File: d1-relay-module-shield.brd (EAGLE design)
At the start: 26.6 x 28.9 mm, 5 parts

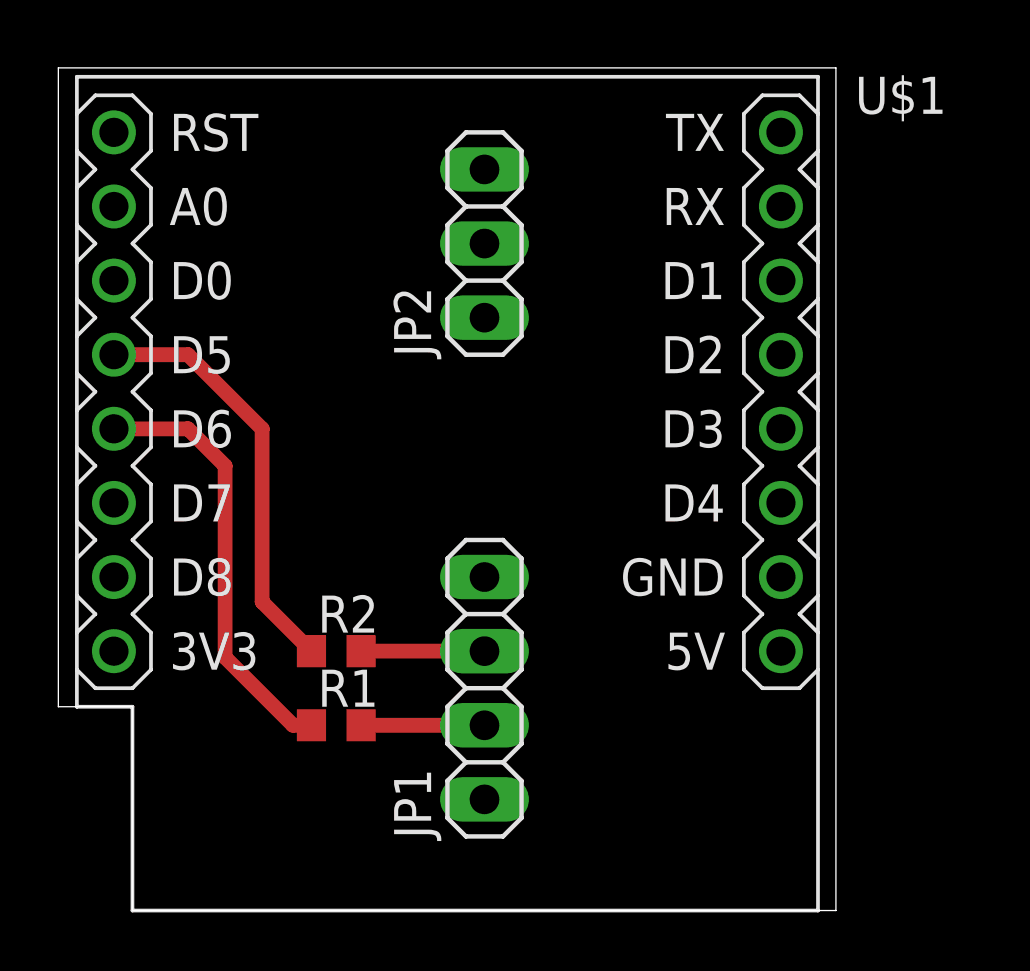
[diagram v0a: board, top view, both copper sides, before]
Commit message: align d1 with edge of relay board and add cutout for jumper
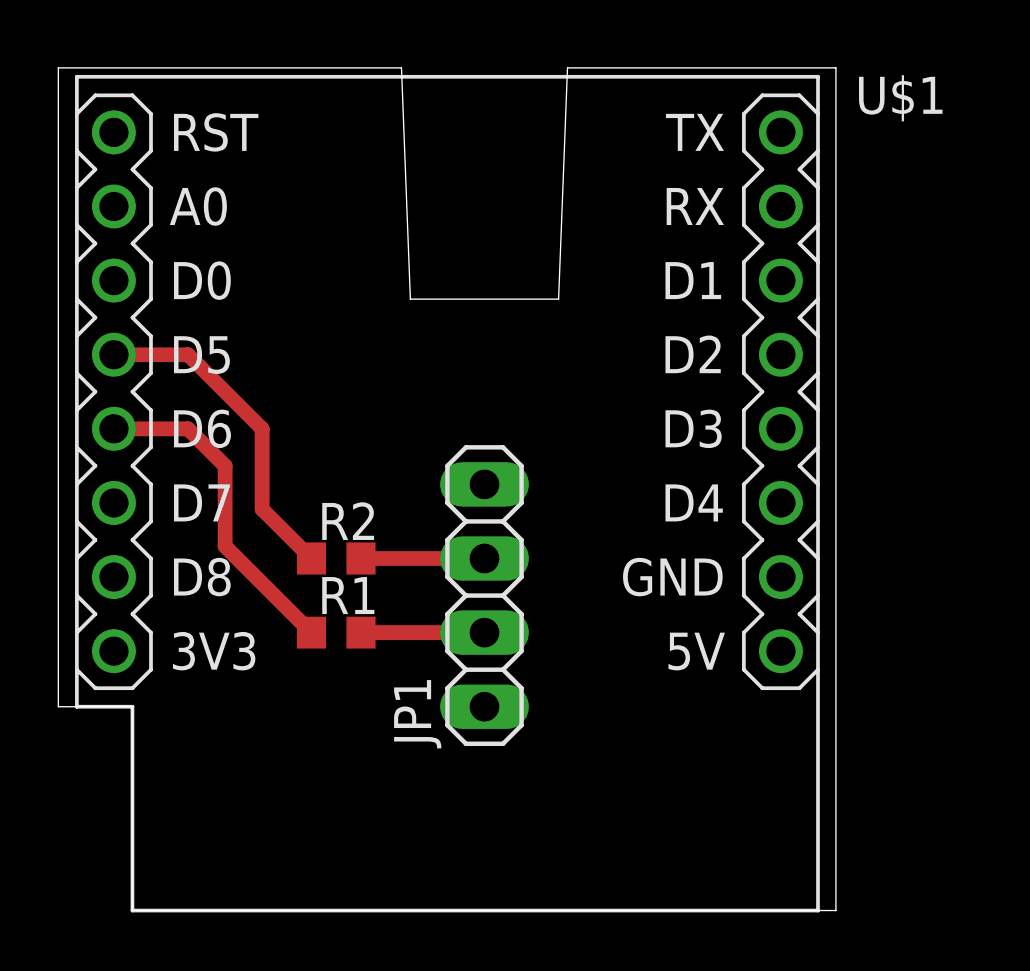
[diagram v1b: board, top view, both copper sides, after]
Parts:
- removed JP2: (no value), pinhead:1X03
- moved R1 3.18 mm to (9.53, 9.53)
- moved JP1 3.17 mm to (14.6, 10.8)
- moved R2 3.17 mm to (9.53, 12.1)
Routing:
- net N$3: track 14.8 -> 11.3 mm
- net N$4: track 14.5 -> 11.3 mm
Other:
- outline, holes or cut-outs redrawn
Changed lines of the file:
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@@
 <wire x1="2.54" y1="0" x2="26.65" y2="0" width="0" layer="20"/>
 <wire x1="26.65" y1="0" x2="26.65" y2="28.88" width="0" layer="20"/>
-<wire x1="26.65" y1="28.88" x2="0" y2="28.88" width="0" layer="20"/>
+<wire x1="26.65" y1="28.88" x2="17.45" y2="28.88" width="0" layer="20"/>
+<wire x1="17.45" y1="28.88" x2="17.145" y2="20.955" width="0" layer="20"/>
+<wire x1="17.145" y1="20.955" x2="12.065" y2="20.955" width="0" layer="20"/>
+<wire x1="12.065" y1="20.955" x2="11.76" y2="28.88" width="0" layer="20"/>
+<wire x1="11.76" y1="28.88" x2="0" y2="28.88" width="0" layer="20"/>
 <wire x1="0" y1="28.88" x2="0" y2="6.985" width="0" layer="20"/>
 <wire x1="0" y1="6.985" x2="2.54" y2="6.985" width="0" layer="20"/>
@@
 </autorouter>
 <elements>
-<element name="JP1" library="pinhead" library_urn="urn:adsk.eagle:library:325" package="1X04" package3d_urn="urn:adsk.eagle:package:22407/2" value="" x="14.605" y="7.62" smashed="yes" rot="R90">
-<attribute name="NAME" x="12.7762" y="2.4638" size="1.27" layer="25" ratio="10" rot="R90"/>
-<attribute name="POPULARITY" value="91" x="46.355" y="26.67" size="1.778" layer="27" rot="R90" display="off"/>
-<attribute name="VALUE" x="17.78" y="2.54" size="1.27" layer="27" rot="R90"/>
-</element>
-<element name="JP2" library="pinhead" library_urn="urn:adsk.eagle:library:325" package="1X03" package3d_urn="urn:adsk.eagle:package:22458/2" value="" x="14.605" y="22.86" smashed="yes" rot="R90">
-<attribute name="NAME" x="12.7762" y="18.9738" size="1.27" layer="25" ratio="10" rot="R90"/>
-<attribute name="POPULARITY" value="92" x="46.355" y="52.07" size="1.778" layer="27" rot="R90" display="off"/>
-<attribute name="VALUE" x="17.78" y="19.05" size="1.27" layer="27" rot="R90"/>
+<element name="JP1" library="pinhead" library_urn="urn:adsk.eagle:library:325" package="1X04" package3d_urn="urn:adsk.eagle:package:22407/2" value="" x="14.605" y="10.795" smashed="yes" rot="R90">
+<attribute name="NAME" x="12.7762" y="5.6388" size="1.27" layer="25" ratio="10" rot="R90"/>
+<attribute name="POPULARITY" value="91" x="46.355" y="29.845" size="1.778" layer="27" rot="R90" display="off"/>
+<attribute name="VALUE" x="17.78" y="5.715" size="1.27" layer="27" rot="R90"/>
 </element>
 <element name="U$1" library="diy-modules" package="WEMOS-D1-MINI-SHIELD" value="WEMOS-D1-MINI-SHIELD" x="13.335" y="14.605" smashed="yes">
@@
 <attribute name="VALUE" x="27.305" y="25.4" size="1.27" layer="27"/>
 </element>
-<element name="R1" library="rcl" library_urn="urn:adsk.eagle:library:334" package="R0603" package3d_urn="urn:adsk.eagle:package:23555/3" value="" x="9.525" y="6.35" smashed="yes">
-<attribute name="NAME" x="8.89" y="6.985" size="1.27" layer="25"/>
-<attribute name="POPULARITY" value="70" x="9.525" y="6.35" size="1.778" layer="27" display="off"/>
-<attribute name="SPICEPREFIX" value="R" x="9.525" y="6.35" size="1.778" layer="27" display="off"/>
-<attribute name="VALUE" x="8.89" y="4.445" size="1.27" layer="27"/>
-</element>
-<element name="R2" library="rcl" library_urn="urn:adsk.eagle:library:334" package="R0603" package3d_urn="urn:adsk.eagle:package:23555/3" value="" x="9.525" y="8.89" smashed="yes">
-<attribute name="NAME" x="8.89" y="9.525" size="1.27" layer="25"/>
-<attribute name="POPULARITY" value="70" x="9.525" y="8.89" size="1.778" layer="27" display="off"/>
-<attribute name="SPICEPREFIX" value="R" x="9.525" y="8.89" size="1.778" layer="27" display="off"/>
-<attribute name="VALUE" x="8.89" y="6.985" size="1.27" layer="27"/>
+<element name="R1" library="rcl" library_urn="urn:adsk.eagle:library:334" package="R0603" package3d_urn="urn:adsk.eagle:package:23555/3" value="" x="9.525" y="9.525" smashed="yes">
+<attribute name="NAME" x="8.89" y="10.16" size="1.27" layer="25"/>
+<attribute name="POPULARITY" value="70" x="9.525" y="9.525" size="1.778" layer="27" display="off"/>
+<attribute name="SPICEPREFIX" value="R" x="9.525" y="9.525" size="1.778" layer="27" display="off"/>
+<attribute name="VALUE" x="8.89" y="7.62" size="1.27" layer="27"/>
+</element>
+<element name="R2" library="rcl" library_urn="urn:adsk.eagle:library:334" package="R0603" package3d_urn="urn:adsk.eagle:package:23555/3" value="" x="9.525" y="12.065" smashed="yes">
+<attribute name="NAME" x="8.89" y="12.7" size="1.27" layer="25"/>
+<attribute name="POPULARITY" value="70" x="9.525" y="12.065" size="1.778" layer="27" display="off"/>
+<attribute name="SPICEPREFIX" value="R" x="9.525" y="12.065" size="1.778" layer="27" display="off"/>
+<attribute name="VALUE" x="8.89" y="10.16" size="1.27" layer="27"/>
 </element>
 </elements>
@@
 <contactref element="U$1" pad="JP1.5"/>
 <contactref element="R1" pad="1"/>
-<wire x1="8.675" y1="6.35" x2="8.04" y2="6.35" width="0.508" layer="1"/>
-<wire x1="8.04" y1="6.35" x2="5.715" y2="8.675" width="0.508" layer="1"/>
-<wire x1="5.715" y1="8.675" x2="5.715" y2="15.24" width="0.508" layer="1"/>
+<wire x1="8.675" y1="9.525" x2="5.715" y2="12.485" width="0.508" layer="1"/>
+<wire x1="5.715" y1="12.485" x2="5.715" y2="15.24" width="0.508" layer="1"/>
 <wire x1="5.715" y1="15.24" x2="4.445" y2="16.51" width="0.508" layer="1"/>
 <wire x1="4.445" y1="16.51" x2="1.905" y2="16.51" width="0.508" layer="1"/>
@@
 <contactref element="U$1" pad="JP1.4"/>
 <contactref element="R2" pad="1"/>
-<wire x1="8.675" y1="8.89" x2="6.985" y2="10.58" width="0.508" layer="1"/>
-<wire x1="6.985" y1="10.58" x2="6.985" y2="16.51" width="0.508" layer="1"/>
+<wire x1="8.675" y1="12.065" x2="6.985" y2="13.755" width="0.508" layer="1"/>
+<wire x1="6.985" y1="13.755" x2="6.985" y2="16.51" width="0.508" layer="1"/>
 <wire x1="6.985" y1="16.51" x2="4.445" y2="19.05" width="0.508" layer="1"/>
 <wire x1="4.445" y1="19.05" x2="1.905" y2="19.05" width="0.508" layer="1"/>
@@
 <contactref element="JP1" pad="2"/>
 <contactref element="R1" pad="2"/>
-<wire x1="10.375" y1="6.35" x2="14.605" y2="6.35" width="0.508" layer="1"/>
+<wire x1="14.605" y1="9.525" x2="10.375" y2="9.525" width="0.508" layer="1"/>
 </signal>
 <signal name="N$2">
 <contactref element="JP1" pad="3"/>
 <contactref element="R2" pad="2"/>
-<wire x1="14.605" y1="8.89" x2="10.375" y2="8.89" width="0.508" layer="1"/>
+<wire x1="14.605" y1="12.065" x2="10.375" y2="12.065" width="0.508" layer="1"/>
 </signal>
 </signals>
